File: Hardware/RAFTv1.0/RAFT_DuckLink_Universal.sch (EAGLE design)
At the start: 68 parts, among them J2 132134-15, J3 132134-15, U10 PE4259, U2 MAX2771ETI+, U6 PE4259, U7 SX1276, U8 PE4259, U9 PE4259

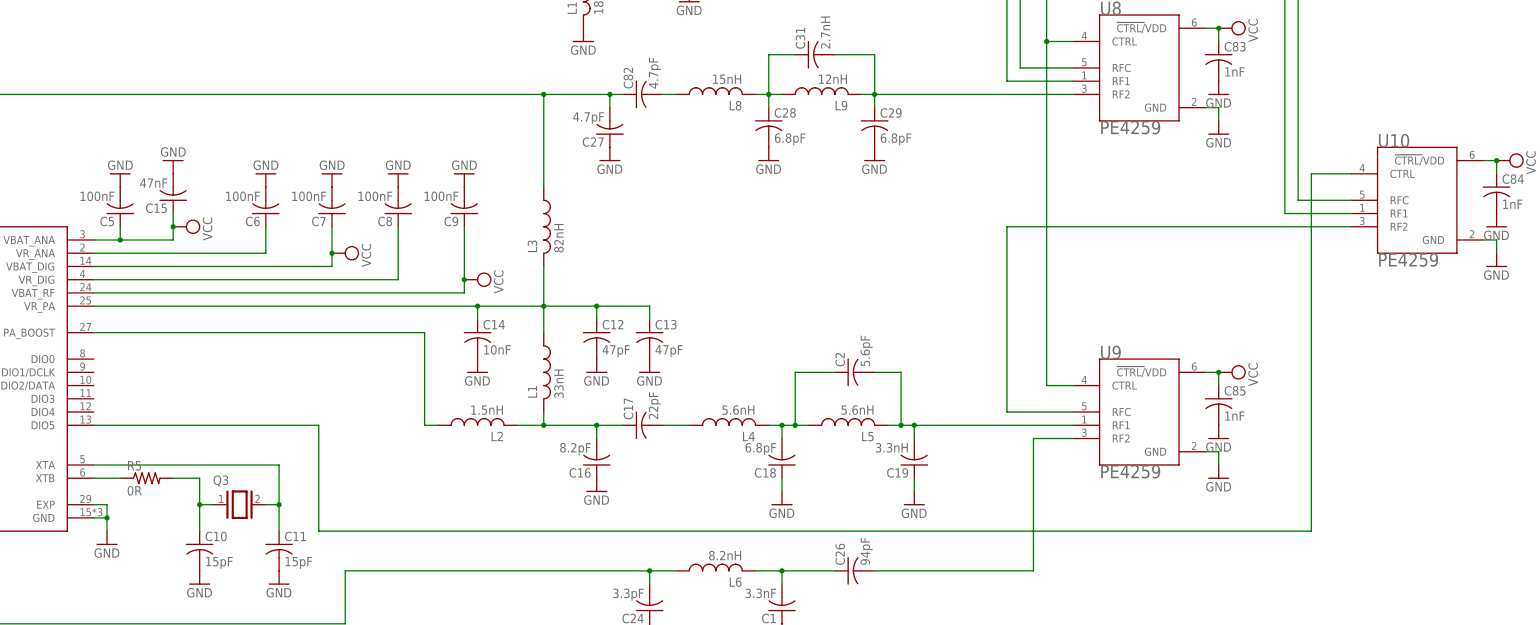
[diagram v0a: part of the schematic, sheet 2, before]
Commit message: rerouted lora rf selector, removed unnecessary resistor
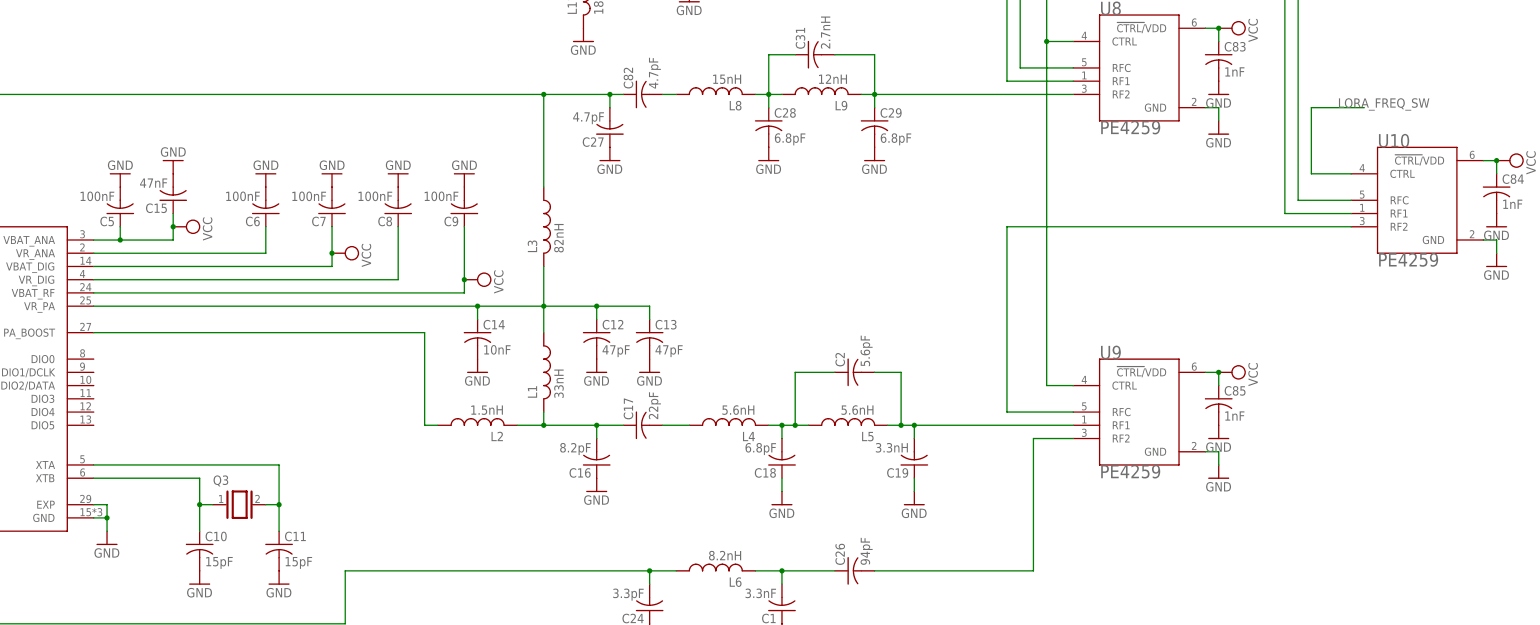
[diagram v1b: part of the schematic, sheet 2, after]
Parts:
- removed R5: 0R, rcl:R-US_R0805
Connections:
- removed net N$13: R5.1, U7.XTB
- removed net N$77: U10.CTRL, U7.DIO5
- new net LORA_FREQ_SW: U10.CTRL
- net N$11: now also U7.XTB; no longer R5.2
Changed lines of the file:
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@@
 <part name="GND53" library="supply1" library_urn="urn:adsk.eagle:library:371" deviceset="GND" device=""/>
 <part name="GND54" library="supply1" library_urn="urn:adsk.eagle:library:371" deviceset="GND" device=""/>
-<part name="R5" library="rcl" library_urn="urn:adsk.eagle:library:334" deviceset="R-US_" device="R0805" package3d_urn="urn:adsk.eagle:package:23553/2" value="0R"/>
 <part name="C12" library="rcl" library_urn="urn:adsk.eagle:library:334" deviceset="C-US" device="C0805" package3d_urn="urn:adsk.eagle:package:23617/2" value="47pF"/>
 <part name="C13" library="rcl" library_urn="urn:adsk.eagle:library:334" deviceset="C-US" device="C0805" package3d_urn="urn:adsk.eagle:package:23617/2" value="47pF"/>
@@
 <attribute name="VALUE" x="167.64" y="-10.16" size="1.778" layer="96"/>
 </instance>
-<instance part="R5" gate="G$1" x="144.78" y="12.7" smashed="yes">
-<attribute name="NAME" x="140.97" y="14.1986" size="1.778" layer="95"/>
-<attribute name="VALUE" x="140.97" y="9.398" size="1.778" layer="96"/>
-</instance>
 <instance part="C12" gate="G$1" x="231.14" y="40.64" smashed="yes">
 <attribute name="NAME" x="232.156" y="41.275" size="1.778" layer="95"/>
@@
 <pinref part="C10" gate="G$1" pin="1"/>
 <wire x1="154.94" y1="7.62" x2="154.94" y2="2.54" width="0.1524" layer="91"/>
-<pinref part="R5" gate="G$1" pin="2"/>
-<wire x1="149.86" y1="12.7" x2="154.94" y2="12.7" width="0.1524" layer="91"/>
+<pinref part="U7" gate="G$1" pin="XTB"/>
+<wire x1="134.62" y1="12.7" x2="154.94" y2="12.7" width="0.1524" layer="91"/>
 <wire x1="154.94" y1="12.7" x2="154.94" y2="7.62" width="0.1524" layer="91"/>
 <junction x="154.94" y="7.62"/>
@@
 <wire x1="170.18" y1="15.24" x2="170.18" y2="7.62" width="0.1524" layer="91"/>
 <junction x="170.18" y="7.62"/>
-</segment>
-</net>
-<net name="N$13" class="0">
-<segment>
-<pinref part="U7" gate="G$1" pin="XTB"/>
-<pinref part="R5" gate="G$1" pin="1"/>
-<wire x1="134.62" y1="12.7" x2="139.7" y2="12.7" width="0.1524" layer="91"/>
 </segment>
 </net>
@@
 </segment>
 </net>
-<net name="N$77" class="0">
-<segment>
-<pinref part="U7" gate="G$1" pin="DIO5"/>
-<wire x1="134.62" y1="22.86" x2="177.8" y2="22.86" width="0.1524" layer="91"/>
-<wire x1="177.8" y1="22.86" x2="177.8" y2="2.54" width="0.1524" layer="91"/>
-<wire x1="177.8" y1="2.54" x2="368.3" y2="2.54" width="0.1524" layer="91"/>
-<wire x1="368.3" y1="2.54" x2="368.3" y2="71.12" width="0.1524" layer="91"/>
+<net name="LORA_FREQ_SW" class="0">
+<segment>
 <pinref part="U10" gate="G$1" pin="CTRL"/>
 <wire x1="368.3" y1="71.12" x2="375.92" y2="71.12" width="0.1524" layer="91"/>
-</segment>
-</net>
+<wire x1="368.3" y1="71.12" x2="368.3" y2="83.82" width="0.1524" layer="91"/>
+<wire x1="368.3" y1="83.82" x2="378.46" y2="83.82" width="0.1524" layer="91"/>
+<label x="373.38" y="83.82" size="1.778" layer="95"/>
+</segment>
+</net>

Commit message: lora rfh changed to low power mode. begin schematic for pa/rfl/rfh universal module
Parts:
- added C20, C21, C22, C23, C3: 100nF, rcl:C-USC0805
- added C25, C30: 15pF, rcl:C-USC0805
- added C46, C47: 47pF, rcl:C-USC0805
- added C48: 10nF, rcl:C-USC0805
- added C49: 47nF, rcl:C-USC0805
- added C50: 8.2pF, rcl:C-USC0805
- added C51: 22pF, rcl:C-USC0805
- added C52: 6.8pF, rcl:C-USC0805
- added C53: 3.3nH, rcl:C-USC0805
- added C54, C63: 1nF, rcl:C-USC0805
- added C55: 2.2pF, rcl:C-USC0805
- added C56, C58, C59: 1.2pF, rcl:C-USC0805
- added C57, C62: 33pF, rcl:C-USC0805
- added C60: 4.7pF, rcl:C-USC0805
- added C61: 1.8pF, rcl:C-USC0805
- added J1: 132134-15, 132134-15:132134-15
- added L10: 1.5nH, rcl:L-USL3225M
- added L13, L7: 33nH, rcl:L-USL3225M
- added L15, L16: 5.6nH, rcl:L-USL3225M
- added L17: 6.8nH, rcl:L-USL3225M
- added L18: 10nH, rcl:L-USL3225M
- added L19, L20: (no value), rcl:L-USL3225M
- added Q1: (no value), special:XTAL/S
- added R5: 0R, rcl:R-US_R0805
- added U1: SX1276, SX1276:SX1276
- added U3, U4: PE4259, PE4259:PE4259
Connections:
- new net LORA_RF_CTRL: U3.CTRL, U4.CTRL
- new net N$13: C30.1, Q1.2, U1.XTA
- new net N$2: C20.1, U1.VR_ANA
- new net N$22: R5.1, U1.XTB
- new net N$23: C46.1, C47.1, C48.1, L13.2, L7.1, U1.VR_PA
- new net N$26: L10.1, U1.PA_BOOST
- new net N$3: C22.1, U1.VR_DIG
- new net N$34: C55.1, C56.1, C57.1, L13.1, U1.RFO_HF(GND)
- new net N$35: C51.2, L15.1
- new net N$36: C52.2, L15.2, L16.1
- new net N$37: C53.2, L16.2, U3.RF2
- new net N$38: C50.2, C51.1, L10.2, L7.2
- new net N$39: C55.2, L17.2, U1.RFI_HF(GND)
- new net N$4: C25.1, Q1.1, R5.2
- new net N$40: C57.2, L18.1
- new net N$41: C58.2, C59.1, C61.2, L19.2, L20.1
- new net N$42: C59.2, C62.2, L20.2, U4.RF2
- new net N$43: C58.1, C60.2, L18.2, L19.1
- new net N$44: J1.SIG, U3.RFC
- new net N$45: U3.RF1, U4.RFC
- new net N$46: U1.RXTX/RF_MOD
- new net N$47: U4.RF1
- net GND: now also C20.2, C21.2, C22.2, C23.2, C25.2, C3.2, C30.2, C46.2, C47.2, C48.2, C49.2, C50.1, C52.1, C53.1, C54.2, C56.2, C60.1, C61.1, C62.1, C63.2, L17.1, U1.EXP, U1.GND, U3.GND, U4.GND
- net MISO: now also U1.MISO
- net MOSI: now also U1.MOSI
- net SPI_CLK: now also U1.SCK
- net SX_CS: now also U1.NSS
- net VCC: now also C21.1, C23.1, C3.1, C49.1, C54.1, C63.1, U1.VBAT_ANA, U1.VBAT_DIG, U1.VBAT_RF, U3.!CTRL/!VDD, U4.!CTRL/!VDD
